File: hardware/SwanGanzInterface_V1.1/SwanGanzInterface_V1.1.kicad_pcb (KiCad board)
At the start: 2 copper layers, 152.4 x 88.9 mm, 108 parts, among them J1 2479774-1, J2 Conn_01x08_Pin, J3 Conn_01x03_Pin, J5 Conn_01x04_Pin, J6 Conn_01x04_Pin, Q1 SQ2389CES-T1_GE3, SW1 Power_Switch, SW2 MODE, SW3 ENTER, U1 LM2937ET-3.3_NOPB, U10 INA122D, U11 OPA2350, U12 INA122D, U13 OPA2350, U2 LM4041CILPR, U3 OPA2350, U4 LP-MSPM0G3507, U5 AdaFruit_1590, U6 Adafruit ST7735R, U7 FT232R, U8 INA122D, U9 OPA2350

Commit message: Added work on FT232, added transmit and receieve leds
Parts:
- removed C9: 0.1u, Capacitor_SMD:C_0603_1608Metric
- removed H5: ~, SGI_FootprintsLib:MountingHole_4_40
- removed JP2: LP_5V_Jumper, SGI_FootprintsLib:PinHeader_1x02_P2.54mm_Vertical
- removed JP3: FT232_3V3_Jumper, SGI_FootprintsLib:PinHeader_1x02_P2.54mm_Vertical
- removed U7: FT232R, SGI_FootprintsLib:FT232R-Breakout
- added J8: 1051640001, SGI_FootprintsLib:1051640001, F.Cu at (251.2, 58.4)
- added R38: 47k, Resistor_SMD:R_0603_1608Metric, F.Cu at (274.9, 57.8)
- added SW4: MODE, SGI_FootprintsLib:SW_PUSH_6mm, F.Cu at (263.6, 67.4)
- added U15: OPA2350, Package_DIP:DIP-8_W7.62mm, F.Cu at (263.1, 78.0)
- added Y1: ABM8AIG-40.000MHZ-12-2Z-T3, SGI_FootprintsLib:ABM8AIG25000MHZ122ZT3, F.Cu at (275.0, 67.9)
- C8: value 0.1u -> 0.01u; moved to F.Cu
- JP1: value LP_3V3_Jumper -> MicroUSB_VBUS
- U4: value LP-MSPM0G3507 -> XM0G3507QPTRQ1; footprint SGI_FootprintsLib:ti_LP_MSPM0G3507 -> SGI_FootprintsLib:MSPM0_PT0048A-IPC_A; moved to F.Cu
- U6: value Adafruit ST7735R -> FT232RL; footprint SGI_FootprintsLib:adafruit_st7735r -> SGI_FootprintsLib:FT232RL
- moved U4 186.0 mm to (267.2, 59.7), turned to 0 degrees
- moved JP1 185.0 mm to (257.2, 65.0), turned to 0 degrees
- moved C8 178.0 mm to (274.9, 55.3)
- moved U6 160.9 mm to (249.8, 68.7), turned to 0 degrees
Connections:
- C12 pad 2: ADC_0.5 -> THERM_LG_ADC_1.1
- C16 pad 2: ADC_0.2 -> P1_LG_ADC_1.3
- C20 pad 2: ADC_1.3 -> P2_LG_ADC_1.5
- C5 pad 1: PB12 -> SW_MODE_PA3
- C7 pad 1: PB13 -> SW_ENTER_PA4
- C8 pad 1: +3V3 -> MSP_NRST
- J2 pad 1: PA10 -> DEBUG1_PA28
- J2 pad 2: PA11 -> DEBUG2_PA31
- J2 pad 3: PA12 -> DEBUG3_PA7
- J2 pad 4: PA13 -> DEBUG4_PA11
- J2 pad 5: PB17 -> DEBUG5_PA12
- J2 pad 6: PA28 -> DEBUG6_PA13
- J2 pad 7: PA31 -> DEBUG7_PA14
- J2 pad 8: PB20 -> DEBUG8_PA22
- JP1 pad 1: Net-(JP1-A) -> +VBUS
- JP1 pad 2: +3V3 -> Net-(J8-VBUS)
- R10 pad 2: PB12 -> SW_MODE_PA3
- R13 pad 2: PB13 -> SW_ENTER_PA4
- R21 pad 2: ADC_0.5 -> THERM_LG_ADC_1.1
- R23 pad 2: ADC_0.7 -> THERM__HG_ADC_1.2
- R28 pad 2: ADC_0.2 -> P1_LG_ADC_1.3
- R30 pad 2: ADC_0.3 -> P1_HG_ADC_1.4
- R35 pad 2: ADC_1.3 -> P2_LG_ADC_1.5
- R37 pad 2: ADC_1.5 -> P2_HG_ADC_1.6
- R7 pad 1: PA15 -> LED_WRK_PB20
- R8 pad 1: PA16 -> LED_ER_PB24
- TP11 pad 1: ADC_0.2 -> P1_LG_ADC_1.3
- TP11 pad 2: ADC_0.2 -> P1_LG_ADC_1.3
- TP12 pad 1: ADC_0.3 -> P1_HG_ADC_1.4
- TP12 pad 2: ADC_0.3 -> P1_HG_ADC_1.4
- TP14 pad 1: ADC_1.3 -> P2_LG_ADC_1.5
- TP14 pad 2: ADC_1.3 -> P2_LG_ADC_1.5
- TP15 pad 1: ADC_1.5 -> P2_HG_ADC_1.6
- TP15 pad 2: ADC_1.5 -> P2_HG_ADC_1.6
- TP8 pad 1: ADC_0.7 -> THERM__HG_ADC_1.2
- TP8 pad 2: ADC_0.7 -> THERM__HG_ADC_1.2
- TP9 pad 1: ADC_0.5 -> THERM_LG_ADC_1.1
- TP9 pad 2: ADC_0.5 -> THERM_LG_ADC_1.1
- U11 pad 1: ADC_0.2 -> P1_LG_ADC_1.3
- U11 pad 5: ADC_0.2 -> P1_LG_ADC_1.3
- U11 pad 7: ADC_0.3 -> P1_HG_ADC_1.4
- U13 pad 1: ADC_1.3 -> P2_LG_ADC_1.5
- U13 pad 5: ADC_1.3 -> P2_LG_ADC_1.5
- U13 pad 7: ADC_1.5 -> P2_HG_ADC_1.6
- U5 pad 10: PB1 -> LCD_WAIT_PB14
- U5 pad 11: PB4 -> LCD_INT_PB16
- U5 pad 12: unconnected-(U5-Y+-Pad12) -> LCD_Y+_A0.1
- U5 pad 13: unconnected-(U5-Y--Pad13) -> LCD_Y-_A0.0
- U5 pad 14: unconnected-(U5-X--Pad14) -> LCD_X-_A0.2
- U5 pad 15: unconnected-(U5-X+-Pad15) -> LCD_X+_A0.3
- U5 pad 5: PB9 -> LCD_SCK_PB9
- U5 pad 6: PB7 -> LCD_POCI_PB7
- U5 pad 7: PB8 -> LCD_PICO_PB8
- U5 pad 8: PB6 -> LCD_CS_PB6
- U5 pad 9: PB15 -> LCD_RST_PB15
- U6 pad 1: GND -> MSP_RX_PA9_FT232_TX
- U6 pad 10: +3V3 -> unconnected-(U6-DCD#-Pad10)
- U6 pad 2: +3V3 -> unconnected-(U6-DTR#-Pad2)
- U6 pad 3: PB15 -> USB_MSP_CTS_PB2_RS232_RTS
- U6 pad 4: PB16 -> FT_+3V3
- U6 pad 5: PB0 -> MSP_TX_PA8_FT232_RX
- U6 pad 6: PB6 -> unconnected-(U6-RI#-Pad6)
- U6 pad 7: PB8 -> GND
- U6 pad 8: PB9 -> unconnected-(U6-NC_1-Pad8)
- U6 pad 9: PB7 -> unconnected-(U6-DSR#-Pad9)
- U9 pad 1: ADC_0.5 -> THERM_LG_ADC_1.1
- U9 pad 5: ADC_0.5 -> THERM_LG_ADC_1.1
- U9 pad 7: ADC_0.7 -> THERM__HG_ADC_1.2
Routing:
- net GND: track 698.0 -> 0.00 mm
- net +3V3: track 508.9 -> 0.00 mm
- net ADC_0.5: track 148.2 -> 0.00 mm, vias 3 -> 0
- net PB9: track 130.6 -> 0.00 mm, vias 6 -> 0
- net ADC_0.7: track 126.4 -> 0.00 mm, vias 2 -> 0
- net UART_Tx: track 101.7 -> 0.00 mm, vias 5 -> 0
- net UART_Rx: track 96.6 -> 0.00 mm, vias 5 -> 0
- net +5V: track 84.6 -> 0.00 mm
- net ADC_1.5: track 82.2 -> 0.00 mm, vias 4 -> 0
- net ADC_1.3: track 78.9 -> 0.00 mm, vias 2 -> 0
- net ADC_0.2: track 77.5 -> 0.00 mm, vias 2 -> 0
- net PA15: track 75.0 -> 0.00 mm, vias 5 -> 0
- net PB1: track 74.5 -> 0.00 mm, vias 4 -> 0
- net PA13: track 70.9 -> 0.00 mm, vias 3 -> 0
- net PB20: track 70.9 -> 0.00 mm, vias 3 -> 0
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
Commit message: Filter paramaters and assigned footprints
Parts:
- removed U15: OPA2350, Package_DIP:DIP-8_W7.62mm
- added C22: 0.1u, Capacitor_SMD:C_0603_1608Metric, F.Cu at (133.4, 65.1)
- added C23: 0.1u, Capacitor_SMD:C_0603_1608Metric, F.Cu at (77.2, 101.9)
- added C24: 0.022u, Capacitor_SMD:C_0805_2012Metric, F.Cu at (83.2, 114.8)
- added C25: 0.022u, Capacitor_SMD:C_0603_1608Metric, F.Cu at (77.2, 104.5)
- added C26: 0.1u, Capacitor_SMD:C_0603_1608Metric, F.Cu at (77.2, 107.0)
- added C27: 3.3n, Capacitor_SMD:C_0603_1608Metric, F.Cu at (174.1, 40.0)
- added C28: 0.1u, Capacitor_SMD:C_0603_1608Metric, F.Cu at (174.1, 42.5)
- added C29: 0.1u, Capacitor_SMD:C_0603_1608Metric, F.Cu at (174.1, 45.0)
- added C30: 4.7u, Capacitor_SMD:C_0805_2012Metric, F.Cu at (174.3, 50.3)
- added C31: 0.1u, Capacitor_SMD:C_0603_1608Metric, F.Cu at (174.1, 47.5)
- added C32: 0.1u, Capacitor_SMD:C_0603_1608Metric, F.Cu at (169.5, 55.1)
- added C33: 1u, Capacitor_SMD:C_0603_1608Metric, F.Cu at (169.5, 57.6)
- added C34: 5u, Capacitor_SMD:C_1206_3216Metric, F.Cu at (174.3, 55.5)
- added C35: 0.1u, Capacitor_SMD:C_0603_1608Metric, F.Cu at (94.6, 60.7)
- added C36: 0.1u, Capacitor_SMD:C_0603_1608Metric, F.Cu at (169.5, 60.1)
- added C37: 1u, Capacitor_SMD:C_0603_1608Metric, F.Cu at (178.1, 40.0)
- added C9: 0.01u, Capacitor_SMD:C_0603_1608Metric, F.Cu at (141.9, 104.5)
- added D4: APHD1608LCGCK, Diode_SMD:D_0603_1608Metric, F.Cu at (141.6, 149.4)
- added D5: APHD1608LSYCK, Diode_SMD:D_0603_1608Metric, F.Cu at (141.6, 152.0)
- added IC1: LM2937ESX-3.3_NOPB, SGI_FootprintsLib:LM2937ESX-3.3_NOPB, F.Cu at (96.1, 113.8)
- added IC2: TSC2046IPWR, SGI_FootprintsLib:SOP65P640X120-16N, F.Cu at (144.0, 144.8)
- added J10: Conn_01x04_Pin, Connector_PinHeader_2.54mm:PinHeader_1x04_P2.54mm_Vertical, F.Cu at (169.8, 41.1)
- added J11: Conn_01x07_Pin, Connector_PinHeader_2.54mm:PinHeader_1x07_P2.54mm_Vertical, F.Cu at (127.0, 135.0)
- added J12: SPKM.28.8.A, TerminalBlock:TerminalBlock_MaiXu_MX126-5.0-02P_1x02_P5.00mm, F.Cu at (96.6, 42.7)
- added J13: Conn_01x06_Pin, Connector_PinHeader_2.54mm:PinHeader_1x06_P2.54mm_Vertical, F.Cu at (165.2, 56.1)
- added J14: Conn_01x03_Pin, Connector_PinHeader_2.54mm:PinHeader_1x03_P2.54mm_Vertical, F.Cu at (150.2, 105.6)
- added J9: 1051640001, SGI_FootprintsLib:1051640001, F.Cu at (135.9, 137.0)
- added R39: 2k, Resistor_SMD:R_0603_1608Metric, F.Cu at (144.5, 136.5)
- added R40: 2k, Resistor_SMD:R_0603_1608Metric, F.Cu at (144.5, 139.0)
- added R41: 750R, Resistor_SMD:R_0603_1608Metric, F.Cu at (178.1, 47.5)
- added R42: 750R, Resistor_SMD:R_0603_1608Metric, F.Cu at (182.1, 40.0)
- added R43: 10k, Resistor_SMD:R_0603_1608Metric, F.Cu at (182.1, 42.5)
- added R44: 19.412k, Resistor_SMD:R_0603_1608Metric, F.Cu at (182.1, 45.0)
- added R45: 100k, Resistor_SMD:R_0603_1608Metric, F.Cu at (182.1, 47.5)
- added R46: 10k, Resistor_SMD:R_0603_1608Metric, F.Cu at (169.5, 62.6)
- added R47: 16.6k, Resistor_SMD:R_0603_1608Metric, F.Cu at (169.5, 65.1)
- added R48: 10k, Resistor_SMD:R_0603_1608Metric, F.Cu at (169.5, 67.6)
- added SW5: ENTER, SGI_FootprintsLib:SW_PUSH_6mm, F.Cu at (126.7, 116.7)
- added U7: INA122D, Package_SO:SOIC-8_5.3x5.3mm_P1.27mm, F.Cu at (136.6, 52.9)
- C10, C14: value 0.1u -> 30p; moved to F.Cu
- C11, C15, C19: footprint Capacitor_SMD:C_1206_3216Metric -> Capacitor_SMD:C_0603_1608Metric
- C12: footprint Capacitor_SMD:C_1206_3216Metric -> Capacitor_SMD:C_0603_1608Metric; moved to F.Cu
- C16: value 0.1u -> 0.022u; footprint Capacitor_SMD:C_1206_3216Metric -> Capacitor_SMD:C_0805_2012Metric
- C17: value 0.1u -> 0.022u; footprint Capacitor_SMD:C_0603_1608Metric -> Capacitor_SMD:C_0805_2012Metric
- C18, C2, C3, C4, Q1, R14, R16: moved to F.Cu
- C20: value 0.1u -> 0.022u; footprint Capacitor_SMD:C_1206_3216Metric -> Capacitor_SMD:C_0603_1608Metric
- C21: value 0.1u -> 0.022u
- C5: value 0.1u -> 1u
- C6: value 0.1u -> 1u; moved to F.Cu
- C7: value 0.1u -> 10u; footprint Capacitor_SMD:C_0603_1608Metric -> Capacitor_SMD:C_1206_3216Metric
- C8: value 0.01u -> 0.47u; footprint Capacitor_SMD:C_0603_1608Metric -> Capacitor_SMD:C_0603_1608Metric_Pad1.08x0.95mm_HandSolder
- J1: value 2479774-1 -> Conn_01x02_Pin; footprint SGI_FootprintsLib:24797741 -> Connector_PinHeader_2.54mm:PinHeader_1x02_P2.54mm_Vertical
- J2: value Conn_01x08_Pin -> Conn_01x09_Pin; footprint Connector_PinHeader_2.54mm:PinHeader_1x08_P2.54mm_Vertical -> Connector_PinSocket_2.54mm:PinSocket_1x09_P2.54mm_Vertical
- J8: value 1051640001 -> Conn_01x04_Pin; footprint SGI_FootprintsLib:1051640001 -> Connector_PinHeader_2.54mm:PinHeader_1x04_P2.54mm_Vertical
- R1: value 5k1 -> 47k
- R11: value 0R -> 100R; moved to F.Cu
- R13: value 100R -> 27k
- R15: value 8k2 -> 27k; moved to F.Cu
- R17: value 65k5 -> 100k; moved to F.Cu
- R18, R19: value 160k -> 10k
- R2: value 5k1 -> 10k
- R21: value 10k -> 8.2k; moved to F.Cu
- R22, R29: value 10k -> 200R
- R23, R4: value 10k -> 100k; moved to F.Cu
- R24, R31: value 200R -> 100k
- R25, R26, R32, R33: value 32k -> 10k
- R28, R35: value 10k -> 17k5; moved to F.Cu
- R3: value 47k -> 1k
- R30: value 17k5 -> 100k; moved to F.Cu
- R36: value 10k -> 1M
- R37: value 17k5 -> 2k; moved to F.Cu
- R38: value 47k -> 0
- R5: value 1k -> 47k; moved to F.Cu
- R6, R8: value 5k -> 100k
- R7: value 5k -> 100R
- SW3: value ENTER -> MODE
- SW4: value MODE -> ENTER
- TP1: value +5V -> +VRef
- TP2: value +3V3 -> +5V
- TP3: value +VRef -> +3V3
- TP8: value T_HG -> T_LG
- TP9: value T_LG -> T_HG
- U1: value LM2937ET-3.3_NOPB -> LM4041CILPR; footprint SGI_FootprintsLib:TO254P470X1028X1955-3P -> SGI_FootprintsLib:ti_LM4041CILPR
- U10, U8: value INA122D -> OPA2350; footprint Package_SO:SOIC-8_5.3x5.3mm_P1.27mm -> Package_DIP:DIP-8_W7.62mm
- U11: value OPA2350 -> FT232RNL; footprint Package_DIP:DIP-8_W7.62mm -> SGI_FootprintsLib:FT232RL
- U12: value INA122D -> MCP34119P; footprint Package_SO:SOIC-8_5.3x5.3mm_P1.27mm -> Package_DIP:DIP-8_W7.62mm_LongPads
- U13: value OPA2350 -> AdaFruit_1590; footprint Package_DIP:DIP-8_W7.62mm -> SGI_FootprintsLib:AdaFruit_1590
- U2: value LM4041CILPR -> OPA2350; footprint SGI_FootprintsLib:ti_LM4041CILPR -> Package_DIP:DIP-8_W7.62mm
- U4: value XM0G3507QPTRQ1 -> XM0G3507QPMRQ1; footprint SGI_FootprintsLib:MSPM0_PT0048A-IPC_A -> SGI_FootprintsLib:PM0064A-IPC_A
- U5: value AdaFruit_1590 -> INA122D; footprint SGI_FootprintsLib:AdaFruit_1590 -> Package_SO:SOIC-8_5.3x5.3mm_P1.27mm
- U6: value FT232RL -> OPA2350; footprint SGI_FootprintsLib:FT232RL -> Package_DIP:DIP-8_W7.62mm
- U9: value OPA2350 -> INA122P; footprint Package_DIP:DIP-8_W7.62mm -> Package_DIP:DIP-8_W7.62mm_LongPads
- moved U6 171.9 mm to (89.5, 130.8)
- moved J1 164.3 mm to (188.4, 41.1), turned to 0 degrees
- moved SW4 142.8 mm to (126.7, 108.1)
- moved D3 141.4 mm to (142.2, 129.0)
- moved Y1 133.0 mm to (150.7, 115.5)
- moved D2 130.5 mm to (134.7, 129.0)
- moved JP1 129.1 mm to (148.8, 135.1)
- moved R8 125.4 mm to (145.9, 107.0), turned to 0 degrees
- moved C7 124.6 mm to (186.0, 55.5), turned to 0 degrees
- moved R7 119.9 mm to (145.9, 104.5), turned to 0 degrees
- moved D1 119.7 mm to (127.2, 129.0)
- moved C5 119.2 mm to (181.1, 55.1), turned to 0 degrees
- moved R6 119.0 mm to (141.9, 117.1), turned to 0 degrees
- moved C6 118.9 mm to (181.1, 57.6), turned to 0 degrees
- moved U4 116.6 mm to (155.7, 93.8)
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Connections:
- net Net-(J8-VBUS) renamed MICRO_VBUS
- C10 pad 2: +3V3 -> HFXIN
- C11 pad 1: Net-(U9A-+) -> SW_UP_PB20
- C12 pad 1: Net-(C12-Pad1) -> SW_ENTER_PB22
- C12 pad 2: THERM_LG_ADC_1.1 -> GND
- C13 pad 1: +3V3 -> SW_DOWN_PB21
- C14 pad 2: +3V3 -> HFXOUT
- C15 pad 1: Net-(U11A-+) -> GND
- C15 pad 2: GND -> +3V3
- C16 pad 1: Net-(C16-Pad1) -> Net-(U6A-+)
- C16 pad 2: P1_LG_ADC_1.3 -> GND
- C17 pad 1: +3V3 -> Net-(C17-Pad1)
- C17 pad 2: GND -> THERM_LG_A0.0
- C18 pad 1: GND -> +3V3
- C18 pad 2: +3V3 -> GND
- C19 pad 1: Net-(U13A-+) -> GND
- C19 pad 2: GND -> +3V3
- C20 pad 1: Net-(C20-Pad1) -> Net-(U8A-+)
- C20 pad 2: P2_LG_ADC_1.5 -> GND
- C21 pad 1: +3V3 -> Net-(C21-Pad1)
- C21 pad 2: GND -> P1_LG_A1.1
- C5 pad 1: SW_MODE_PA3 -> GND
- C5 pad 2: GND -> Net-(U4-PA23_VREF+)
- C6 pad 1: BACKLITE -> +3V3
- C7 pad 1: SW_ENTER_PA4 -> +3V3
- C8 pad 1: MSP_NRST -> Net-(U4-VCORE)
- J1 pad 1: unconnected-(J1-MH1-Pad1) -> +VBUS
- J1 pad 2: unconnected-(J1-MH2-Pad2) -> GND
- J2 pad 1: DEBUG1_PA28 -> DBG1_PB14
- J2 pad 2: DEBUG2_PA31 -> DBG2_PB15
- J2 pad 3: DEBUG3_PA7 -> DBG3_PB16
- J2 pad 4: DEBUG4_PA11 -> DBG4_PA12
- J2 pad 5: DEBUG5_PA12 -> DBG5_PA13
- J2 pad 6: DEBUG6_PA13 -> DBG6_PA22
- J2 pad 7: DEBUG7_PA14 -> DBG7_PA24
- J2 pad 8: DEBUG8_PA22 -> DBG8_PB25
- J8 pad 2: USB_D- -> USB_D+
- J8 pad 3: USB_D+ -> USB_D-
- J8 pad 4: unconnected-(J8-ID-Pad4) -> GND
- R1 pad 1: Net-(J1-CC1) -> +VRef
- R1 pad 2: GND -> Net-(R1-Pad2)
- R10 pad 2: SW_MODE_PA3 -> SW_ENTER_PB22
- R11 pad 1: +3V3 -> Net-(R11-Pad1)
- R11 pad 2: BACKLITE -> SW_DOWN_PB21
- R12 pad 1: +3V3 -> Therm_Voltage+
- R12 pad 2: Net-(R12-Pad2) -> Net-(U5--IN)
- R13 pad 1: Net-(R12-Pad2) -> Net-(U5--IN)
- R13 pad 2: SW_ENTER_PA4 -> GND
- R14 pad 1: +3V3 -> Therm_Voltage+
- R14 pad 2: Net-(U8--IN) -> Net-(J3-Pin_2)
- R15 pad 1: Net-(U8--IN) -> Net-(U5-RG+)
- R15 pad 2: GND -> Net-(U5-RG-)
- R16 pad 1: +3V3 -> Therm__InstrOut
- R16 pad 2: Net-(J3-Pin_2) -> Net-(C17-Pad1)
- R17 pad 1: Net-(U8-RG+) -> Net-(C17-Pad1)
- R17 pad 2: Net-(U8-RG-) -> Net-(U6A-+)
- R18 pad 1: Therm__InstrOut -> GND
- R18 pad 2: Net-(C12-Pad1) -> Net-(U6A--)
- R19 pad 1: Net-(C12-Pad1) -> Net-(U6A--)
- R19 pad 2: Net-(U9A-+) -> THERM_LG_A0.0
- R2 pad 1: Net-(J1-CC2) -> Net-(R1-Pad2)
- R20 pad 2: Net-(U9A--) -> Net-(U6B--)
- R21 pad 1: Net-(U9A--) -> Net-(U6B--)
- R21 pad 2: THERM_LG_ADC_1.1 -> THERM__HG_A0.1
- R22 pad 1: GND -> Net-(U7-RG+)
- R22 pad 2: Net-(U9B--) -> Net-(U7-RG-)
- R23 pad 1: Net-(U9B--) -> P1__InstrOut
- R23 pad 2: THERM__HG_ADC_1.2 -> Net-(C21-Pad1)
- R24 pad 1: Net-(U10-RG+) -> Net-(C21-Pad1)
- R24 pad 2: Net-(U10-RG-) -> Net-(U8A-+)
- R25 pad 1: P1__InstrOut -> GND
- R25 pad 2: Net-(C16-Pad1) -> Net-(U8A--)
- R26 pad 1: Net-(C16-Pad1) -> Net-(U8A--)
- R26 pad 2: Net-(U11A-+) -> P1_LG_A1.1
- R27 pad 2: Net-(U11A--) -> Net-(U8B--)
- R28 pad 1: Net-(U11A--) -> Net-(U8B--)
- R28 pad 2: P1_LG_ADC_1.3 -> P1_HG_A1.2
- R29 pad 1: GND -> Net-(U9-RG+)
- R29 pad 2: Net-(U11B--) -> Net-(U9-RG-)
- R3 pad 1: +VRef -> +3V3
- R3 pad 2: Net-(R3-Pad2) -> +VRef
- R30 pad 1: Net-(U11B--) -> P2__InstrOut
- R30 pad 2: P1_HG_ADC_1.4 -> Net-(C25-Pad1)
- R31 pad 1: Net-(U12-RG+) -> Net-(C25-Pad1)
- R31 pad 2: Net-(U12-RG-) -> Net-(U10A-+)
- R32 pad 1: P2__InstrOut -> GND
- R32 pad 2: Net-(C20-Pad1) -> Net-(U10A--)
- R33 pad 1: Net-(C20-Pad1) -> Net-(U10A--)
- R33 pad 2: Net-(U13A-+) -> P2_LG_A1.4
- R34 pad 2: Net-(U13A--) -> Net-(U10B--)
- R35 pad 1: Net-(U13A--) -> Net-(U10B--)
- R35 pad 2: P2_LG_ADC_1.5 -> P2_HG_A1.5
- R36 pad 1: GND -> USB_MP
- R36 pad 2: Net-(U13B--) -> GND
- R37 pad 1: Net-(U13B--) -> +3V3
- R37 pad 2: P2_HG_ADC_1.6 -> Net-(D1-A)
- R38 pad 1: +3V3 -> Net-(J10-Pin_1)
- R38 pad 2: MSP_NRST -> +3V3
- R4 pad 1: Net-(R3-Pad2) -> GND
- R4 pad 2: GND -> Net-(U4-PA2_ROSC)
- R5 pad 2: +VRef -> MSP_NRST
- R6 pad 2: Net-(D1-A) -> Net-(R6-Pad2)
- R7 pad 1: LED_WRK_PB20 -> Net-(R6-Pad2)
- R7 pad 2: Net-(D2-A) -> SW_UP_PB20
- R8 pad 1: LED_ER_PB24 -> +3V3
- R8 pad 2: Net-(D3-A) -> Net-(R10-Pad1)
- R9 pad 2: Net-(R10-Pad1) -> Net-(R11-Pad1)
- SW2 pad 2: Net-(R10-Pad1) -> MSP_NRST
- SW3 pad 2: Net-(R12-Pad2) -> Net-(R6-Pad2)
- SW4 pad 2: MSP_NRST -> Net-(R10-Pad1)
- TP1 pad 1: +5V -> +VRef
- TP1 pad 2: +5V -> +VRef
- TP11 pad 1: P1_LG_ADC_1.3 -> P1_LG_A1.1
- TP11 pad 2: P1_LG_ADC_1.3 -> P1_LG_A1.1
- TP12 pad 1: P1_HG_ADC_1.4 -> P1_HG_A1.2
- TP12 pad 2: P1_HG_ADC_1.4 -> P1_HG_A1.2
- TP14 pad 1: P2_LG_ADC_1.5 -> P2_LG_A1.4
- TP14 pad 2: P2_LG_ADC_1.5 -> P2_LG_A1.4
- TP15 pad 1: P2_HG_ADC_1.6 -> P2_HG_A1.5
- TP15 pad 2: P2_HG_ADC_1.6 -> P2_HG_A1.5
- TP2 pad 1: +3V3 -> +5V
- TP2 pad 2: +3V3 -> +5V
- TP3 pad 1: +VRef -> +3V3
- TP3 pad 2: +VRef -> +3V3
- TP8 pad 1: THERM__HG_ADC_1.2 -> THERM_LG_A0.0
- TP8 pad 2: THERM__HG_ADC_1.2 -> THERM_LG_A0.0
- TP9 pad 1: THERM_LG_ADC_1.1 -> THERM__HG_A0.1
- TP9 pad 2: THERM_LG_ADC_1.1 -> THERM__HG_A0.1
- U1 pad 1: +5V -> Net-(R1-Pad2)
- U1 pad 2: GND -> +VRef
- U1 pad 3: +3V3 -> GND
- U10 pad 1: Net-(U10-RG+) -> P2_LG_A1.4
- U10 pad 2: P1_SIG- -> Net-(U10A--)
- U10 pad 3: P1_SIG+ -> Net-(U10A-+)
- U10 pad 5: GND -> P2_LG_A1.4
- U10 pad 6: P1__InstrOut -> Net-(U10B--)
- U10 pad 7: +3V3 -> P2_HG_A1.5
- U10 pad 8: Net-(U10-RG-) -> +3V3
- U11 pad 1: P1_LG_ADC_1.3 -> MSP_RX_PA1_FT_TX
- U11 pad 2: Net-(U11A--) -> unconnected-(U11-DTR#-Pad2)
- U11 pad 3: Net-(U11A-+) -> MSP_CTS_PB26_FT_RTS
- U11 pad 4: GND -> FT_+3V3
- U11 pad 5: P1_LG_ADC_1.3 -> MSP_TX_PA28_FT_RX
- U11 pad 6: Net-(U11B--) -> unconnected-(U11-RI#-Pad6)
- U11 pad 7: P1_HG_ADC_1.4 -> GND
- U11 pad 8: +3V3 -> unconnected-(U11-NC_1-Pad8)
- U12 pad 1: Net-(U12-RG+) -> SPEAK_CD_PA14
- U12 pad 2: P2_SIG- -> Net-(U12-FC2)
- U12 pad 3: P2_SIG+ -> Net-(U12-FC1)
- U12 pad 4: GND -> Net-(U12-VIN)
- U12 pad 5: GND -> Net-(J12-SIG+)
- U12 pad 6: P2__InstrOut -> +3V3
- U12 pad 7: +3V3 -> GND
- U12 pad 8: Net-(U12-RG-) -> Net-(J12-SIG-)
- U13 pad 1: P2_LG_ADC_1.5 -> +3V3
- U13 pad 2: Net-(U13A--) -> GND
- U13 pad 3: Net-(U13A-+) -> unconnected-(U13-3V0-Pad3)
- U13 pad 4: GND -> LCD_LITE_PB13
- U13 pad 5: P2_LG_ADC_1.5 -> LCD_SCK_PB9
- U13 pad 6: Net-(U13B--) -> LCD_POCI_PB7
- U13 pad 7: P2_HG_ADC_1.6 -> LCD_PICO_PB8
- U13 pad 8: +3V3 -> LCD_CS_PB6
- U2 pad 1: Net-(R3-Pad2) -> P1_VCC
- U2 pad 2: +VRef -> P1_VCC
- U2 pad 3: GND -> +VRef
- U3 pad 1: P1_VCC -> Therm_Voltage+
- U3 pad 2: P1_VCC -> Therm_Voltage+
- U3 pad 6: P2_VCC -> Touch_VRef
- U3 pad 7: P2_VCC -> Touch_VRef
- U4 pad 1: unconnected-(U4-PA0_FCC_IN-Pad1) -> LCD_LITE_PB13
- U4 pad 10: SW_ENTER_PA4 -> P1_HG_A1.2
- U4 pad 11: HFXIN -> unconnected-(U4-PA18_A1_3-Pad11)
- U4 pad 12: HFXOUT -> SWDIO_PA19
- U4 pad 13: DEBUG3_PA7 -> SWCLK_PA20
- U4 pad 14: USB_MSP_CTS_PB2_RS232_RTS -> P2_LG_A1.4
- U4 pad 15: USB_MSP_RTS_PB3_RS232_CTS -> P2_HG_A1.5
- U4 pad 16: MSP_TX_PA8_FT232_RX -> unconnected-(U4-PB19_A1_6-Pad16)
- U4 pad 17: MSP_RX_PA9_FT232_TX -> GND
- U4 pad 18: USB_CONN_PA10 -> DBG6_PA22
- U4 pad 19: DEBUG4_PA11 -> SW_UP_PB20
- U4 pad 2: unconnected-(U4-PA1-Pad2) -> DBG1_PB14
- U4 pad 20: LCD_CS_PB6 -> SW_DOWN_PB21
- U4 pad 21: LCD_POCI_PB7 -> SW_ENTER_PB22
- U4 pad 22: LCD_PICO_PB8 -> LED_WRK_PB23
- U4 pad 23: LCD_SCK_PB9 -> LED_ER_PB24
- U4 pad 24: LCD_WAIT_PB14 -> Net-(U4-PA23_VREF+)
- U4 pad 25: LCD_RST_PB15 -> DBG7_PA24
- U4 pad 26: LCD_INT_PB16 -> DBG8_PB25
- U4 pad 27: DEBUG5_PA12 -> MSP_RTS_PB25_FT_CTS
- U4 pad 28: DEBUG6_PA13 -> MSP_CTS_PB26_FT_RTS
- U4 pad 29: DEBUG7_PA14 -> unconnected-(U4-PB27-Pad29)
- U4 pad 3: DEBUG1_PA28 -> DBG2_PB15
- U4 pad 30: SPEAK_DAC -> THERM__HG_A0.1
- U4 pad 31: THERM_LG_ADC_1.1 -> THERM_LG_A0.0
- U4 pad 32: THERM__HG_ADC_1.2 -> Net-(U4-VCORE)
- U4 pad 33: P1_LG_ADC_1.3 -> unconnected-(U4-PA0_FCC_IN-Pad33)
- U4 pad 34: SWDIO -> MSP_RX_PA1_FT_TX
- U4 pad 35: SWCLK -> MSP_TX_PA28_FT_RX
- U4 pad 36: P1_HG_ADC_1.4 -> FT_RST_PA29
- U4 pad 37: P2_LG_ADC_1.5 -> USB_CONN_PA30
- U4 pad 38: P2_HG_ADC_1.6 -> MSP_NRST
- U4 pad 39: GND -> unconnected-(U4-PA31_CLK_OUT-Pad39)
- U4 pad 4: MSP_NRST -> DBG3_PB16
- U4 pad 40: DEBUG8_PA22 -> +3V3
- U4 pad 41: LED_WRK_PB20 -> GND
- U4 pad 42: LED_ER_PB24 -> Net-(U4-PA2_ROSC)
- U4 pad 43: Net-(U4-PA23_VREF+) -> unconnected-(U4-PA3_LFXIN-Pad43)
- U4 pad 44: LCD_X+_A0.3 -> unconnected-(U4-PA4_LFCLK_IN_LFXOUT-Pad44)
- U4 pad 45: LCD_X-_A0.2 -> HFXIN
- U4 pad 46: LCD_Y+_A0.1 -> HFXOUT
- U4 pad 47: LCD_Y-_A0.0 -> unconnected-(U4-PB0-Pad47)
- U4 pad 48: Net-(U4-VCORE) -> unconnected-(U4-PB1-Pad48)
- U4 pad 5: DEBUG2_PA31 -> DBG4_PA12
- U4 pad 6: +3V3 -> DBG5_PA13
- U4 pad 7: GND -> SPEAK_CD_PA14
- U4 pad 8: Net-(U4-PA2_ROSC) -> SPEAK_DAC_PA15
- U4 pad 9: SW_MODE_PA3 -> P1_LG_A1.1
- U5 pad 1: +3V3 -> Net-(U5-RG+)
- U5 pad 2: GND -> Net-(U5--IN)
- U5 pad 3: unconnected-(U5-3V0-Pad3) -> Net-(J3-Pin_2)
- U5 pad 4: BACKLITE -> GND
- U5 pad 5: LCD_SCK_PB9 -> GND
- U5 pad 6: LCD_POCI_PB7 -> Therm__InstrOut
- U5 pad 7: LCD_PICO_PB8 -> +3V3
- U5 pad 8: LCD_CS_PB6 -> Net-(U5-RG-)
- U6 pad 1: MSP_RX_PA9_FT232_TX -> THERM_LG_A0.0
- U6 pad 2: unconnected-(U6-DTR#-Pad2) -> Net-(U6A--)
- U6 pad 3: USB_MSP_CTS_PB2_RS232_RTS -> Net-(U6A-+)
- U6 pad 4: FT_+3V3 -> GND
- U6 pad 5: MSP_TX_PA8_FT232_RX -> THERM_LG_A0.0
- U6 pad 6: unconnected-(U6-RI#-Pad6) -> Net-(U6B--)
- U6 pad 7: GND -> THERM__HG_A0.1
- U6 pad 8: unconnected-(U6-NC_1-Pad8) -> +3V3
- U8 pad 1: Net-(U8-RG+) -> P1_LG_A1.1
- U8 pad 2: Net-(U8--IN) -> Net-(U8A--)
- U8 pad 3: Net-(J3-Pin_2) -> Net-(U8A-+)
- U8 pad 5: GND -> P1_LG_A1.1
- U8 pad 6: Therm__InstrOut -> Net-(U8B--)
- U8 pad 7: +3V3 -> P1_HG_A1.2
- U8 pad 8: Net-(U8-RG-) -> +3V3
- U9 pad 1: THERM_LG_ADC_1.1 -> Net-(U9-RG+)
- U9 pad 2: Net-(U9A--) -> P2_SIG-
- U9 pad 3: Net-(U9A-+) -> P2_SIG+
- U9 pad 5: THERM_LG_ADC_1.1 -> GND
- U9 pad 6: Net-(U9B--) -> P2__InstrOut
- U9 pad 7: THERM__HG_ADC_1.2 -> +3V3
- U9 pad 8: +3V3 -> Net-(U9-RG-)
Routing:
- net Therm__InstrOut: vias 1 -> 0
- net THERM__HG_ADC_1.2: vias 2 -> 0
- net THERM_LG_ADC_1.1: vias 3 -> 0
- net SW_MODE_PA3: vias 3 -> 0
- net SW_ENTER_PA4: vias 1 -> 0
- net P2__InstrOut: vias 1 -> 0
- net P2_VCC: vias 2 -> 0
- net P2_SIG+: vias 3 -> 0
- net P2_LG_ADC_1.5: vias 2 -> 0
- net P2_HG_ADC_1.6: vias 4 -> 0
- net P1__InstrOut: vias 1 -> 0
- net P1_VCC: vias 1 -> 0
- net P1_SIG+: vias 3 -> 0
- net P1_LG_ADC_1.3: vias 2 -> 0
- net P1_HG_ADC_1.4: vias 1 -> 0
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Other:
- board outline removed
- board text removed: "Pressure 1"
- board text removed: "Pressure 2"
- board text removed: "S1"
- board text removed: "Swan Ganz Interface v1.1 Ashton Knecht Nathan DeLaRosa Jack Son Jerry Xia Dr. Valvano"
- board text removed: "Thermistor"

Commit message: Block Diagram for Layout
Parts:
- moved U13 275.4 mm to (288.0, 188.6), turned to 90 degrees
- moved C10 187.9 mm to (368.8, 49.8)
- moved C11 187.9 mm to (329.5, 96.8)
- moved C12 187.9 mm to (329.5, 99.3)
- moved C13 187.9 mm to (329.5, 101.8)
- moved C14 187.9 mm to (368.8, 52.3)
- moved C16 187.9 mm to (282.4, 131.7)
- moved C17 187.9 mm to (282.4, 134.7)
- moved C2 187.9 mm to (305.7, 105.2)
- moved C24 187.9 mm to (270.8, 104.5)
- moved C27 187.9 mm to (361.7, 29.8)
- moved C28 187.9 mm to (361.7, 32.3)
- moved C29 187.9 mm to (361.7, 34.8)
- moved C31 187.9 mm to (361.7, 37.3)
- moved C35 187.9 mm to (282.2, 50.5)
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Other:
- board outline added: 177.8 x 101.6 mm
- copper layers 2 -> 4
- board text added: "Ashton"
- board text added: "Buttons - Joypad Layout"
- board text added: "FT232 and Power"
- board text added: "Front - Horizontal Traces Back - Vertical Traces"
- board text added: "Jack"
- board text added: "LCD Driver"
- board text added: "MSPM0+"
- board text added: "Make sure this is centered"
- board text added: "Micro-USB"
- board text added: "Pressure 1"
- board text added: "Pressure 2"
- board text added: "Programming Pins"
- board text added: "RST Button"
- board text added: "Speaker Driver"
- board text added: "Thermistor"
- board text added: "Touch Screen Driver"
- board text added: "User 1: Block Diagram"
- board text added: "Voltage Reference"

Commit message: Layout Part 1
Pressure, Audio, Thermistor
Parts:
- removed C1, C11, C12, C13, C28, C29, C3, C31, C35, C4: 0.1u, Capacitor_SMD:C_0603_1608Metric
- removed C2: 10u, Capacitor_SMD:C_1206_3216Metric
- removed C27: 3.3n, Capacitor_SMD:C_0603_1608Metric
- removed C30: 4.7u, Capacitor_SMD:C_0805_2012Metric
- removed C37: 1u, Capacitor_SMD:C_0603_1608Metric
- removed C9: 0.01u, Capacitor_SMD:C_0603_1608Metric
- removed D1: +3V3, SGI_FootprintsLib:LED_D5.0mm
- removed D2: WORKING, SGI_FootprintsLib:LED_D5.0mm
- removed D3: ERROR, SGI_FootprintsLib:LED_D5.0mm
- removed D4: APHD1608LCGCK, Diode_SMD:D_0603_1608Metric
- removed D5: APHD1608LSYCK, Diode_SMD:D_0603_1608Metric
- removed IC1: LM2937ESX-3.3_NOPB, SGI_FootprintsLib:LM2937ESX-3.3_NOPB
- removed IC2: TSC2046IPWR, SGI_FootprintsLib:SOP65P640X120-16N
- removed J1: Conn_01x02_Pin, Connector_PinHeader_2.54mm:PinHeader_1x02_P2.54mm_Vertical
- removed J10, J8: Conn_01x04_Pin, Connector_PinHeader_2.54mm:PinHeader_1x04_P2.54mm_Vertical
- removed J11: Conn_01x07_Pin, Connector_PinHeader_2.54mm:PinHeader_1x07_P2.54mm_Vertical
- removed J13: Conn_01x06_Pin, Connector_PinHeader_2.54mm:PinHeader_1x06_P2.54mm_Vertical
- removed JP1: MicroUSB_VBUS, SGI_FootprintsLib:PinHeader_1x02_P2.54mm_Vertical
- removed Q1: SQ2389CES-T1_GE3, Package_TO_SOT_SMD:SOT-23
- removed R1, R5: 47k, Resistor_SMD:R_0603_1608Metric
- removed R10, R11, R7: 100R, Resistor_SMD:R_0603_1608Metric
- removed R2, R43: 10k, Resistor_SMD:R_0603_1608Metric
- removed R3: 1k, Resistor_SMD:R_0603_1608Metric
- removed R36: 1M, Resistor_SMD:R_0603_1608Metric
- removed R37, R39, R40: 2k, Resistor_SMD:R_0603_1608Metric
- removed R38: 0, Resistor_SMD:R_0603_1608Metric
- removed R41, R42: 750R, Resistor_SMD:R_0603_1608Metric
- removed R44: 19.412k, Resistor_SMD:R_0603_1608Metric
- removed R45, R6, R8, R9: 100k, Resistor_SMD:R_0603_1608Metric
- removed SW1: Power_Switch, SGI_FootprintsLib:SW-T3-1A-A-A3-S1
- removed SW2, SW3: MODE, SGI_FootprintsLib:SW_PUSH_6mm
- removed SW4, SW5: ENTER, SGI_FootprintsLib:SW_PUSH_6mm
- removed TP1: +VRef, SGI_FootprintsLib:Testpoint_1x02_P2.54mm
- removed TP2: +5V, SGI_FootprintsLib:Testpoint_1x02_P2.54mm
- removed TP3: +3V3, SGI_FootprintsLib:Testpoint_1x02_P2.54mm
- removed TP4: +VBUS, SGI_FootprintsLib:Testpoint_1x02_P2.54mm
- removed TP5, TP6: GND, SGI_FootprintsLib:Testpoint_1x02_P2.54mm
- removed U1: LM4041CILPR, SGI_FootprintsLib:ti_LM4041CILPR
- removed U11: FT232RNL, SGI_FootprintsLib:FT232RL
- removed U13: AdaFruit_1590, SGI_FootprintsLib:AdaFruit_1590
- removed U2, U3: OPA2350, Package_DIP:DIP-8_W7.62mm
- U5, U7: value INA122D -> INA122P; footprint Package_SO:SOIC-8_5.3x5.3mm_P1.27mm -> Package_DIP:DIP-8_W7.62mm_LongPads
- moved C10 298.7 mm to (70.6, 67.2)
- moved C14 298.7 mm to (70.6, 69.7)
- moved C5 298.7 mm to (70.6, 62.2)
- moved C6 298.7 mm to (70.6, 64.7)
- moved C8 298.7 mm to (74.8, 65.5)
- moved R4 298.7 mm to (70.6, 72.2)
- moved C7 298.7 mm to (75.4, 62.6)
- moved J2 298.0 mm to (28.4, 54.3)
- moved J14 279.1 mm to (60.0, 69.0)
- moved C34 262.4 mm to (99.9, 31.6)
- moved R46 259.9 mm to (97.5, 38.1), turned to 180 degrees
- moved C32 259.6 mm to (97.5, 42.6)
- moved R47 256.9 mm to (100.8, 37.0), turned to -90 degrees
- moved C33 256.8 mm to (100.7, 34.0)
- moved R48 248.7 mm to (109.0, 40.4)
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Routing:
- net GND: track 0.00 -> 199.7 mm, vias 0 -> 10
- net P2_HG_A1.5: track 0.00 -> 96.7 mm, vias 0 -> 3
- net +3V3: track 0.00 -> 88.5 mm, vias 0 -> 5
- net P2_LG_A1.4: track 0.00 -> 66.8 mm, vias 0 -> 1
- net P2__InstrOut: track 0.00 -> 62.0 mm
- net P1_LG_A1.1: track 0.00 -> 39.7 mm, vias 0 -> 1
- net THERM_LG_A0.0: track 0.00 -> 39.1 mm, vias 0 -> 2
- net Net-(J12-SIG-): track 0.00 -> 26.2 mm
- net Therm__InstrOut: track 0.00 -> 24.8 mm
- net P1_HG_A1.2: track 0.00 -> 22.2 mm
- net Net-(J3-Pin_2): track 0.00 -> 21.3 mm
- net THERM__HG_A0.1: track 0.00 -> 17.0 mm
- net Net-(U10A-+): track 0.00 -> 16.5 mm, vias 0 -> 1
- net P1__InstrOut: track 0.00 -> 15.7 mm, vias 0 -> 1
- net SPEAK_CD_PA14: track 0.00 -> 14.6 mm
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
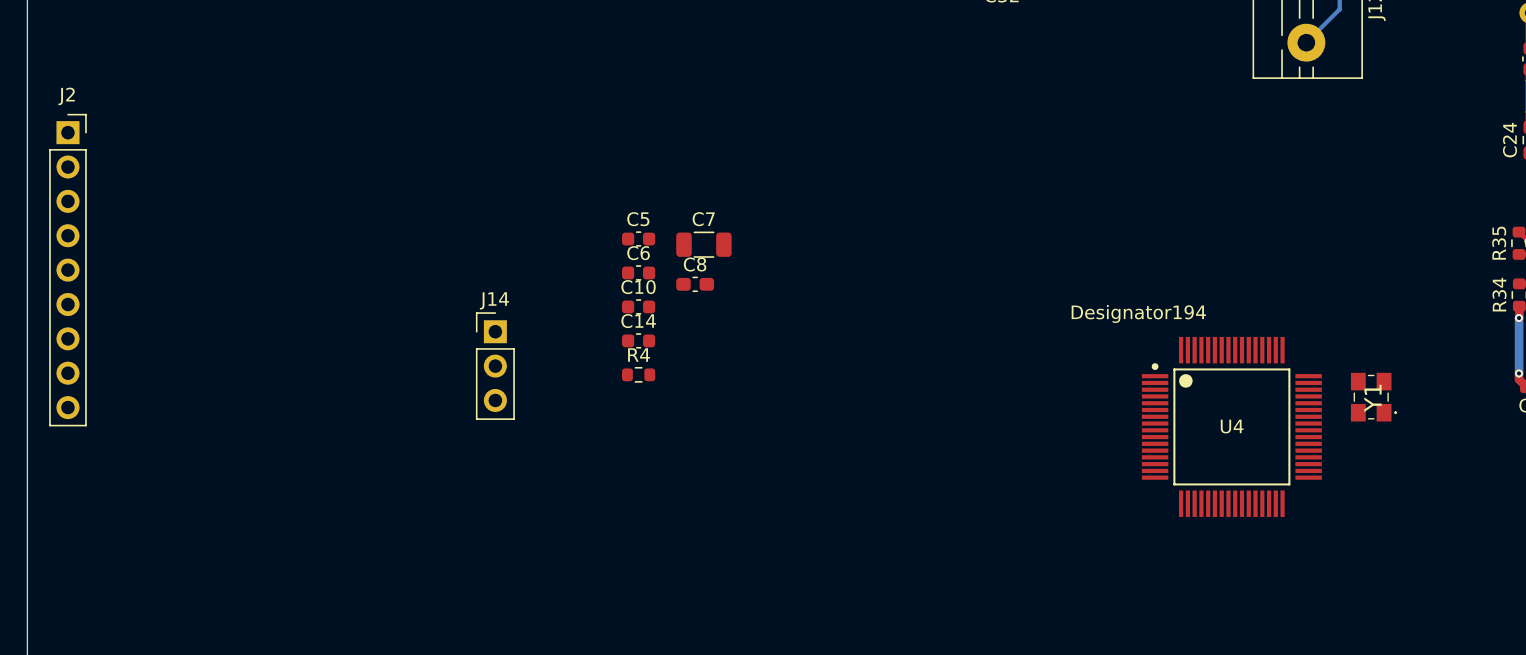
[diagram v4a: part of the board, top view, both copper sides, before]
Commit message: Started MCU layout
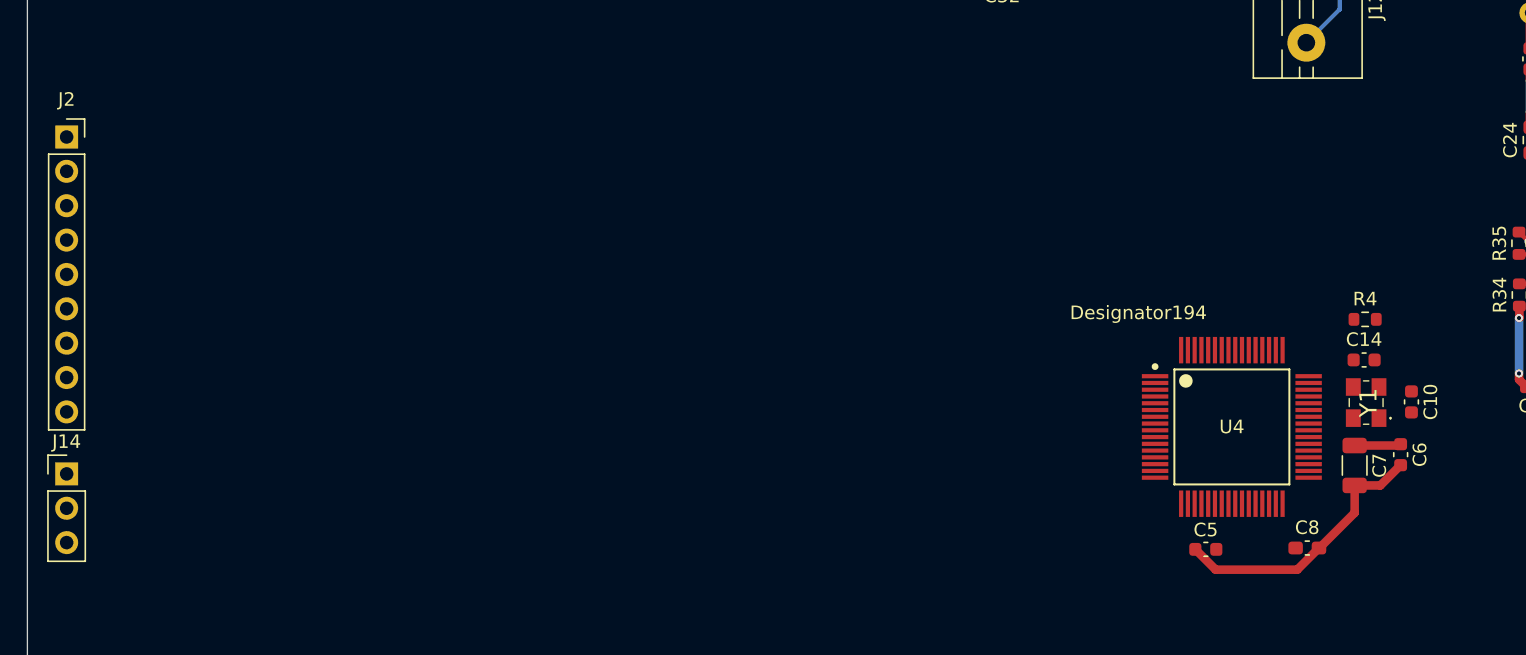
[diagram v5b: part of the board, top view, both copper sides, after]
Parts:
- moved C6 57.9 mm to (126.9, 78.1), turned to -90 degrees
- moved C10 57.6 mm to (127.7, 74.2), turned to -90 degrees
- moved R4 53.9 mm to (124.3, 68.1), turned to 180 degrees
- moved C14 53.6 mm to (124.2, 71.1), turned to 180 degrees
- moved C7 50.8 mm to (123.5, 78.9), turned to -90 degrees
- moved C8 49.3 mm to (120.0, 85.0)
- moved C5 47.8 mm to (112.5, 85.1)
- moved J14 33.4 mm to (28.3, 79.5)
- moved Y1 0.55 mm to (124.3, 74.2)
- moved J2 0.34 mm to (28.3, 54.6)
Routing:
- net GND: track 199.7 -> 219.9 mm
- net +3V3: track 88.5 -> 92.0 mm
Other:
- board text added: "Maybe reduce traces to pads down to around 0.2mm"
